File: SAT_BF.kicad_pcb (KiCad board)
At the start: 2 copper layers, 8 parts, among them U2 ZC323200, U3 module_mpu6050, U4 HMC5883L, U7 INA219, U8 module_bme280

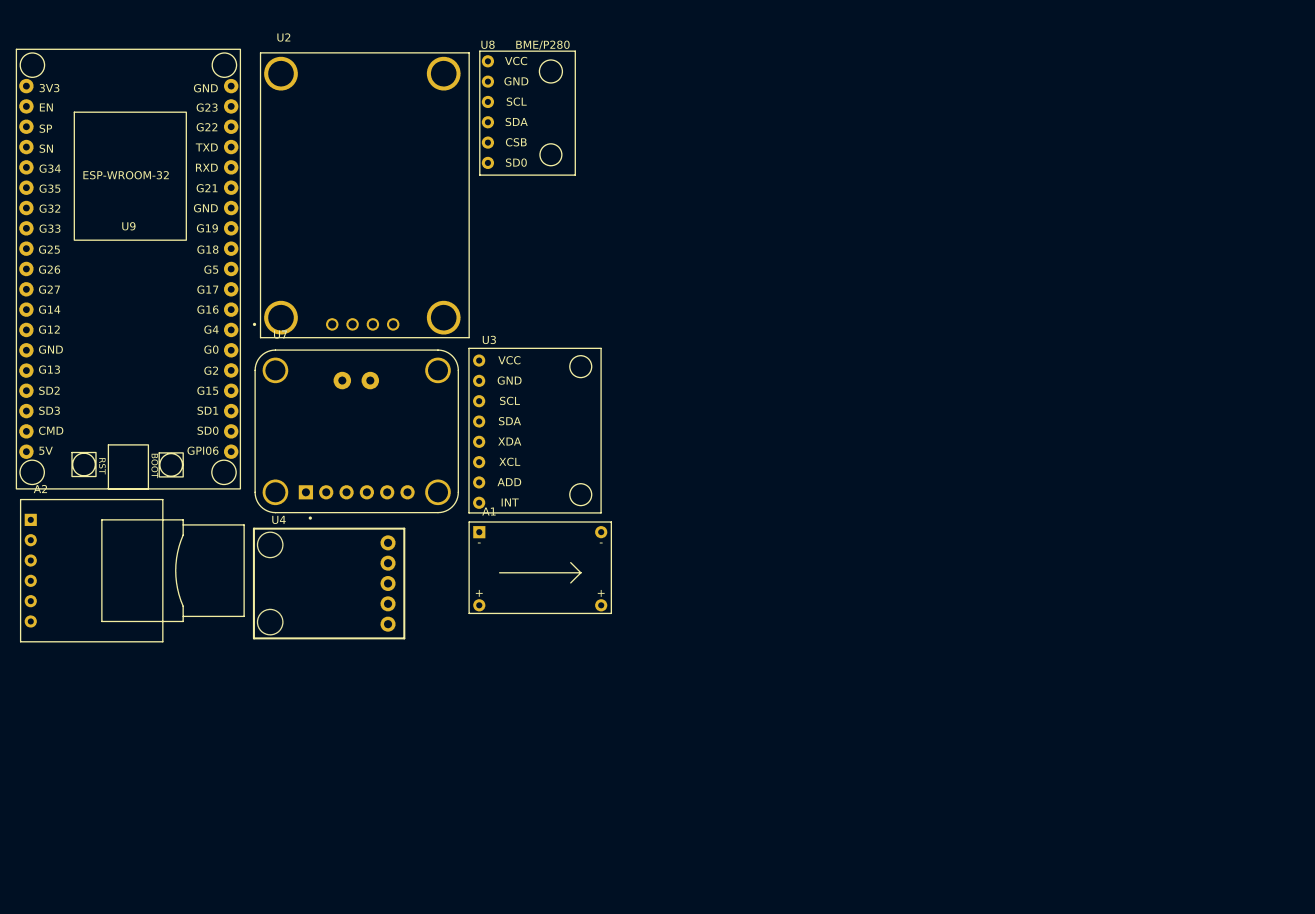
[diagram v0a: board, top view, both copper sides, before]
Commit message: Adicionando Wemmos D1 e atualizando a PCI
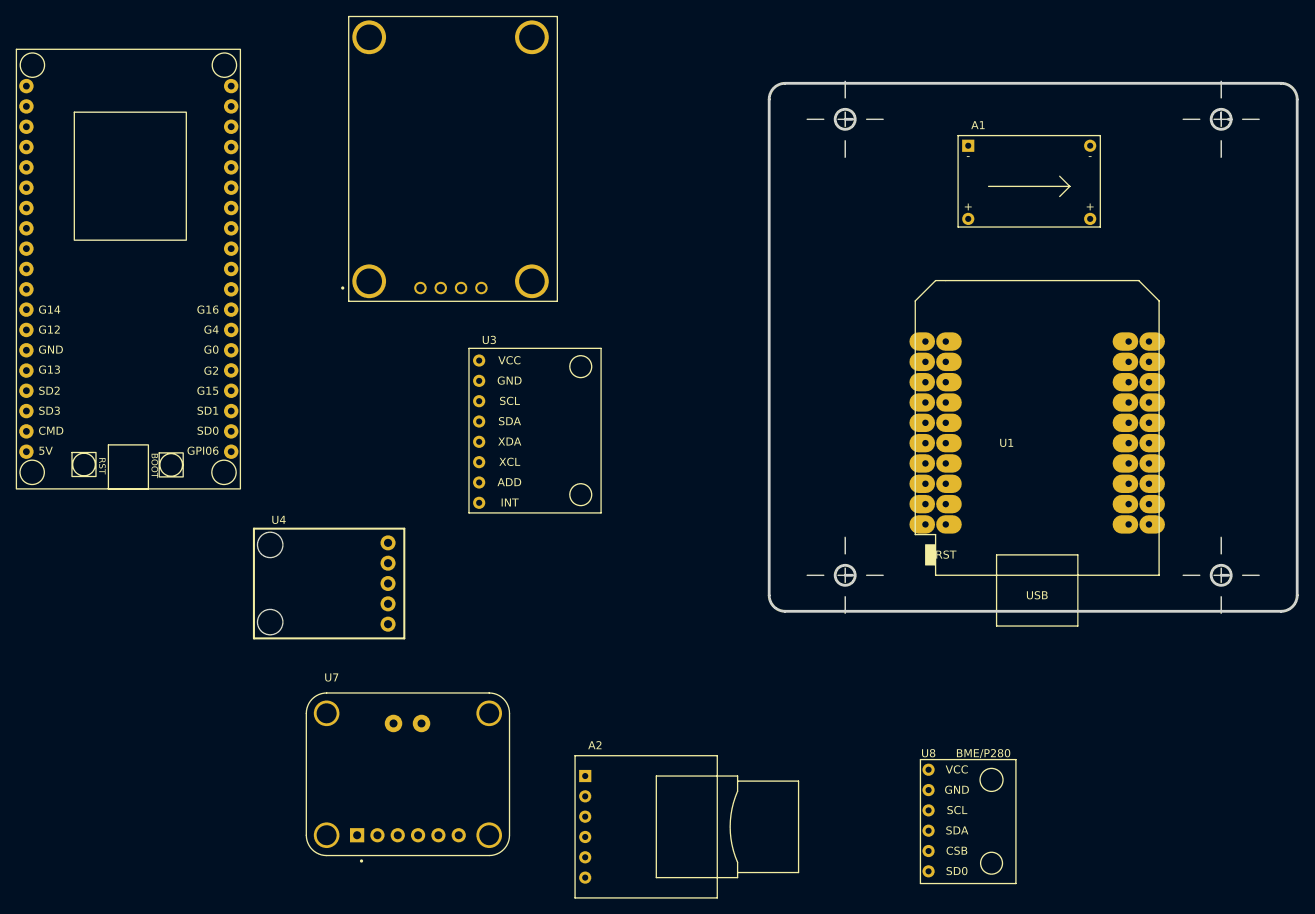
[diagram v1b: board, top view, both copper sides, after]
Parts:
- added U1: esp32-wemos-d1-mini, esp32-wemos-d1-mini:esp32-wemos-d1-mini, F.Cu at (201.0, 91.5)
- U9: value ~ -> esp32_38pins
- moved U8 104.3 mm to (192.5, 146.0)
- moved A1 77.9 mm to (192.4, 55.6)
- moved A2 76.3 mm to (144.5, 134.3)
- moved U7 43.3 mm to (122.3, 134.1)
- moved U2 11.9 mm to (128.1, 57.2)
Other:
- board outline added: 66 x 66.5 mm

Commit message: atualizações no esquematico
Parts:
- moved U9 169.4 mm to (256.8, 78.9)
- moved A1 134.7 mm to (60.0, 80.4)
- moved U8 126.0 mm to (68.1, 165.8)
- moved U2 101.1 mm to (131.7, 158.2)
- moved U3 97.9 mm to (44.0, 144.6)
- moved U7 94.3 mm to (67.6, 57.3)
- moved A2 92.6 mm to (140.4, 41.8)
- moved U1 50.7 mm to (151.9, 78.8)
- moved U4 38.3 mm to (83.9, 135.7)
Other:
- board size 66 x 66.5 mm -> 151.4 x 144 mm

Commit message: trazendo atualizações
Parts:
- added REF**: PinHeader_2x20_P2.00mm_Vertical, Connector_PinHeader_2.00mm:PinHeader_2x20_P2.00mm_Vertical, F.Cu at (40.0, 128.5)
- moved U3 128.0 mm to (172.0, 147.7)
- moved U1 117.6 mm to (65.5, 158.6)
- moved U8 92.0 mm to (160.1, 166.4)
- moved A2 74.3 mm to (72.5, 72.0), turned to -90 degrees
- moved A1 44.7 mm to (58.4, 125.1)
- moved U4 37.9 mm to (120.6, 126.5)
- moved U7 0.98 mm to (67.3, 56.4)
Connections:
- U1 pad 1: unconnected-(U1-GND-Pad1) -> /GND
- U1 pad 10: unconnected-(U1-IO_19/D6-Pad10) -> /SPI_MISO_1
- U1 pad 14: unconnected-(U1-IO_05/D8-Pad14) -> /NSS_LORA
- U1 pad 16: unconnected-(U1-3V3-Pad16) -> /3V3
- U1 pad 18: unconnected-(U1-IO_13/TCK-Pad18) -> /CS_SDCARD
- U1 pad 22: unconnected-(U1-GND-Pad22) -> /GND
- U1 pad 24: unconnected-(U1-IO_27-Pad24) -> /I2C_SCL_2
- U1 pad 25: unconnected-(U1-IO_22/D1/SCL-Pad25) -> /I2C_SCL_1
- U1 pad 27: unconnected-(U1-IO_21/D2/SDA-Pad27) -> /I2C_SDA_1
- U1 pad 28: unconnected-(U1-IO_32-Pad28) -> /RX_RS422
- U1 pad 29: unconnected-(U1-IO_17/D3-Pad29) -> /RX_GPS
- U1 pad 31: unconnected-(U1-IO_16/D4-Pad31) -> /TX_GPS
- U1 pad 32: unconnected-(U1-IO_04-Pad32) -> /LORA_DIO0
- U1 pad 33: unconnected-(U1-GND-Pad33) -> /GND
- U1 pad 36: unconnected-(U1-IO_02-Pad36) -> /LORA_RST
- U1 pad 8: unconnected-(U1-IO_18/D5-Pad8) -> /SPI_SCK_1
- U1 pad 9: unconnected-(U1-IO_33-Pad9) -> /TX_RS422

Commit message: adicionando os barramentos
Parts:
- removed the REF** at (40.0, 128.5)
- removed U2: ZC323200, ZC323200:XCVR_ZC323200
- removed U9: esp32_38pins, CTE_KICADMOD09_ESP32_38PIN:ESP-32_38PIN
- added A1: Mini360_Module, Charleslabs_Parts:Mini360_Module, F.Cu at (62.7, 44.8)
- added REF**: PinHeader_2x20_P2.54mm_Vertical, Connector_PinHeader_2.54mm:PinHeader_2x20_P2.54mm_Vertical, F.Cu at (41.0, 121.9)
- added REF**: PinHeader_2x20_P2.54mm_Vertical, Connector_PinHeader_2.54mm:PinHeader_2x20_P2.54mm_Vertical, F.Cu at (204.2, 43.9)
- added REF**: PinHeader_2x20_P2.54mm_Vertical, Connector_PinHeader_2.54mm:PinHeader_2x20_P2.54mm_Vertical, F.Cu at (44.0, 43.9)
- moved A2 164.3 mm to (236.8, 72.5)
- moved U7 163.3 mm to (230.6, 53.1)
- moved U3 80.9 mm to (160.0, 67.8)
- moved U8 76.5 mm to (151.1, 90.4)
- moved U4 71.8 mm to (137.9, 56.8)
- moved U1 14.8 mm to (78.3, 151.1), turned to -90 degrees
- moved A1 10.6 mm to (68.0, 120.5)
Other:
- board size 151.4 x 144 mm -> 229.2 x 144.5 mm
- board text added: "A1"
